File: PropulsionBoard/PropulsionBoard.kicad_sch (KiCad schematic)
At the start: 0 parts

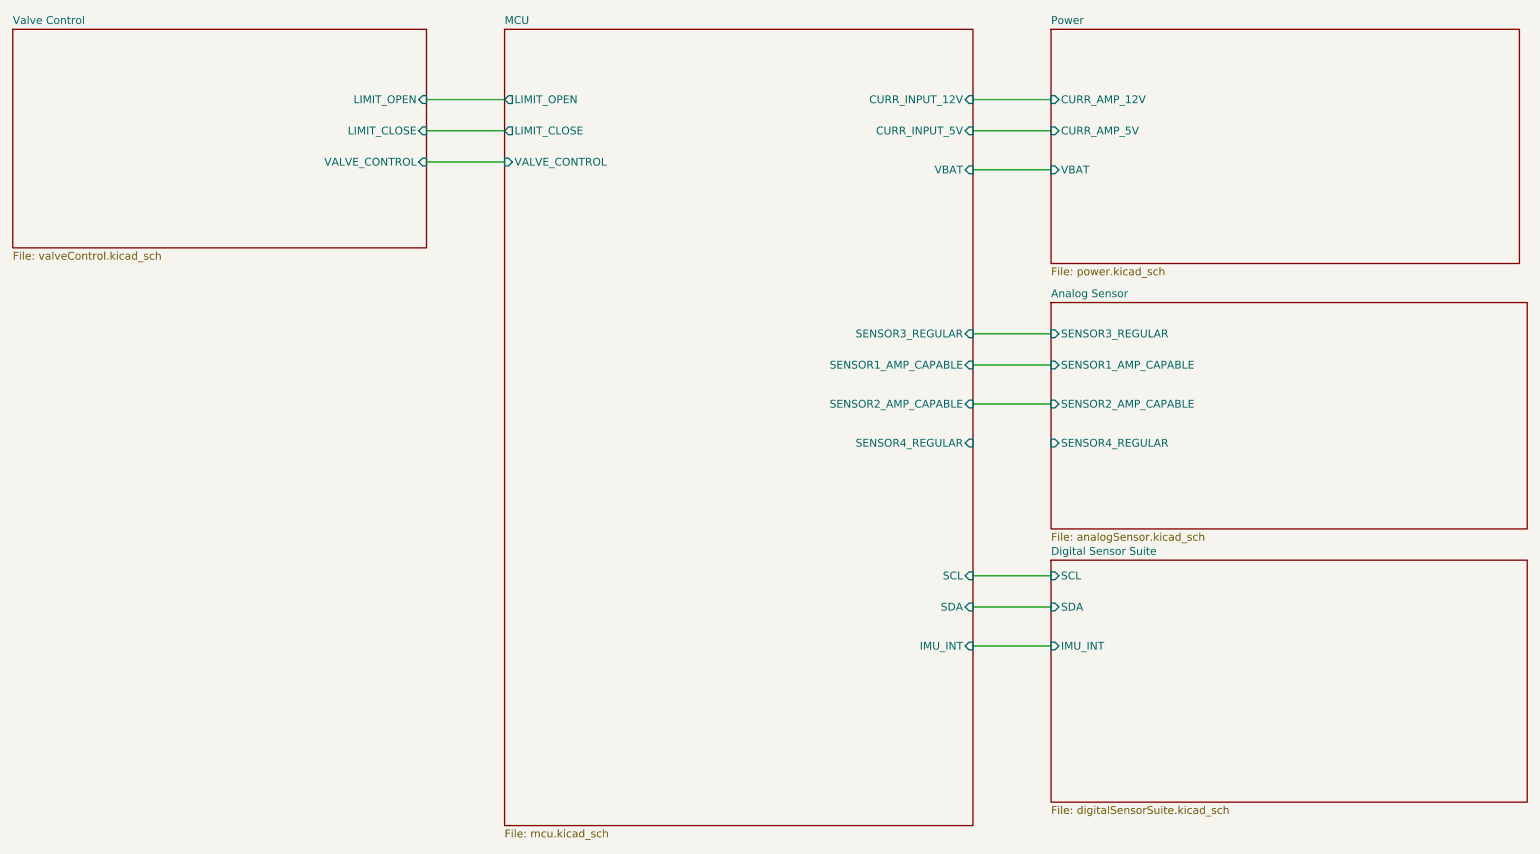
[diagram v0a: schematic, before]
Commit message: propulsion board address second review changes
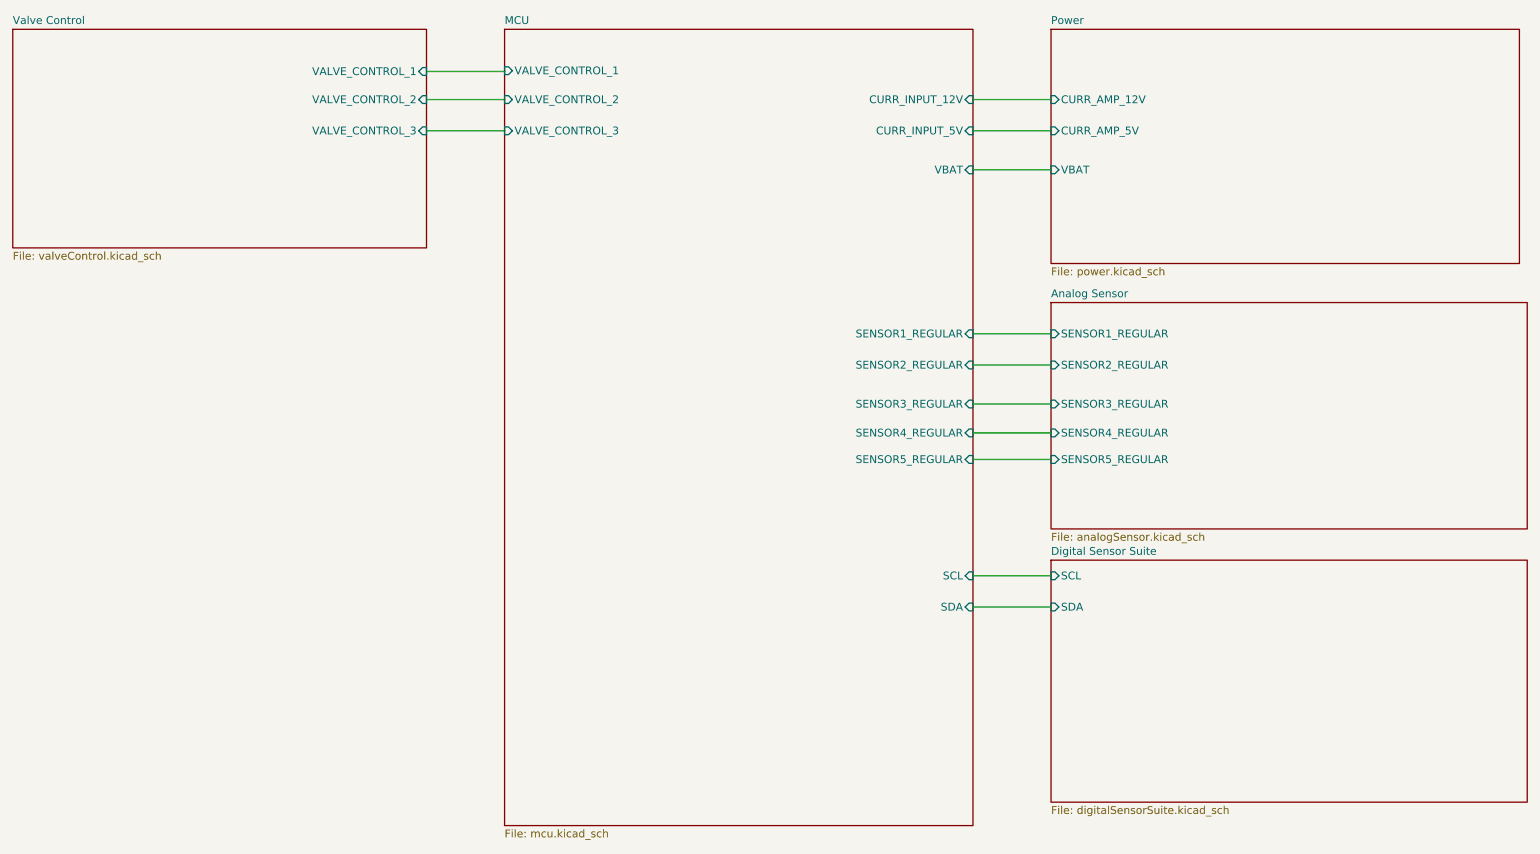
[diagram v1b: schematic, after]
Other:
- sheet Analog Sensor ports: added SENSOR1_REGULAR, SENSOR2_REGULAR, SENSOR5_REGULAR; removed SENSOR1_AMP_CAPABLE, SENSOR2_AMP_CAPABLE
- sheet Digital Sensor Suite ports: added none; removed IMU_INT
- sheet MCU ports: added SENSOR1_REGULAR, SENSOR2_REGULAR, SENSOR5_REGULAR, VALVE_CONTROL_1, VALVE_CONTROL_2, VALVE_CONTROL_3; removed IMU_INT, LIMIT_CLOSE, LIMIT_OPEN, SENSOR1_AMP_CAPABLE, SENSOR2_AMP_CAPABLE, VALVE_CONTROL
- sheet Valve Control ports: added VALVE_CONTROL_1, VALVE_CONTROL_2, VALVE_CONTROL_3; removed LIMIT_CLOSE, LIMIT_OPEN, VALVE_CONTROL
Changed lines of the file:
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@@
+    (stroke (width 0) (type default))
+  )
+  (wire (pts (xy 184.15 95.377) (xy 196.85 95.377))
+    (stroke (width 0) (type default))
+  )
+  (wire (pts (xy 184.15 91.059) (xy 196.85 91.059))
     (stroke (width 0) (type default))
   )
@@
   )
   (wire (pts (xy 184.15 36.83) (xy 196.85 36.83))
+    (stroke (width 0) (type default))
+  )
+  (wire (pts (xy 107.95 32.258) (xy 107.95 32.131))
     (stroke (width 0) (type default))
   )
@@
     (stroke (width 0) (type default))
   )
-  (wire (pts (xy 95.25 46.99) (xy 107.95 46.99))
-    (stroke (width 0) (type default))
-  )
-  (wire (pts (xy 184.15 125.73) (xy 196.85 125.73))
+  (wire (pts (xy 95.25 32.258) (xy 107.95 32.258))
     (stroke (width 0) (type default))
   )
@@
     (property "Sheetfile" "digitalSensorSuite.kicad_sch" (at 196.85 151.7146 0)
       (effects (font (size 1.27 1.27)) (justify left top))
-    )
-    (pin "IMU_INT" input (at 196.85 125.73 180)
-      (effects (font (size 1.27 1.27)) (justify left))
     )
     (pin "SDA" input (at 196.85 119.38 180)
@@
       (effects (font (size 1.27 1.27)) (justify left top))
     )
-    (pin "VALVE_CONTROL" input (at 95.25 46.99 0)
+    (pin "VALVE_CONTROL_3" input (at 95.25 41.91 0)
       (effects (font (size 1.27 1.27)) (justify right))
     )
-    (pin "LIMIT_OPEN" input (at 95.25 36.83 0)
+    (pin "VALVE_CONTROL_2" input (at 95.25 36.83 0)
       (effects (font (size 1.27 1.27)) (justify right))
     )
-    (pin "LIMIT_CLOSE" input (at 95.25 41.91 0)
+    (pin "VALVE_CONTROL_1" input (at 95.25 32.258 0)
       (effects (font (size 1.27 1.27)) (justify right))
     )
@@
       (effects (font (size 1.27 1.27)) hide)
     )
-    (pin "LIMIT_CLOSE" output (at 107.95 41.91 180)
-      (effects (font (size 1.27 1.27)) (justify left))
-    )
-    (pin "VALVE_CONTROL" input (at 107.95 46.99 180)
-      (effects (font (size 1.27 1.27)) (justify left))
-    )
-    (pin "SENSOR3_REGULAR" input (at 184.15 74.93 0)
+    (pin "SENSOR1_REGULAR" input (at 184.15 74.93 0)
       (effects (font (size 1.27 1.27)) (justify right))
     )
-    (pin "SENSOR1_AMP_CAPABLE" input (at 184.15 80.01 0)
+    (pin "SENSOR2_REGULAR" input (at 184.15 80.01 0)
       (effects (font (size 1.27 1.27)) (justify right))
     )
-    (pin "SENSOR2_AMP_CAPABLE" input (at 184.15 86.36 0)
+    (pin "SENSOR3_REGULAR" input (at 184.15 86.36 0)
       (effects (font (size 1.27 1.27)) (justify right))
     )
-    (pin "SENSOR4_REGULAR" input (at 184.15 92.71 0)
+    (pin "SENSOR4_REGULAR" input (at 184.15 91.059 0)
       (effects (font (size 1.27 1.27)) (justify right))
     )
@@
       (effects (font (size 1.27 1.27)) (justify right))
     )
-    (pin "IMU_INT" input (at 184.15 125.73 0)
+    (pin "VALVE_CONTROL_3" input (at 107.95 41.91 180)
+      (effects (font (size 1.27 1.27)) (justify left))
+    )
+    (pin "VALVE_CONTROL_2" input (at 107.95 36.83 180)
+      (effects (font (size 1.27 1.27)) (justify left))
+    )
+    (pin "VALVE_CONTROL_1" input (at 107.95 32.131 180)
+      (effects (font (size 1.27 1.27)) (justify left))
+    )
+    (pin "SENSOR5_REGULAR" input (at 184.15 95.377 0)
       (effects (font (size 1.27 1.27)) (justify right))
-    )
-    (pin "LIMIT_OPEN" output (at 107.95 36.83 180)
-      (effects (font (size 1.27 1.27)) (justify left))
     )
     (instances
@@
       (effects (font (size 1.27 1.27)) (justify left top))
     )
-    (pin "SENSOR1_AMP_CAPABLE" input (at 196.85 80.01 180)
+    (pin "SENSOR2_REGULAR" input (at 196.85 80.01 180)
       (effects (font (size 1.27 1.27)) (justify left))
     )
-    (pin "SENSOR3_REGULAR" input (at 196.85 74.93 180)
+    (pin "SENSOR1_REGULAR" input (at 196.85 74.93 180)
       (effects (font (size 1.27 1.27)) (justify left))
     )
-    (pin "SENSOR2_AMP_CAPABLE" input (at 196.85 86.36 180)
+    (pin "SENSOR3_REGULAR" input (at 196.85 86.36 180)
       (effects (font (size 1.27 1.27)) (justify left))
     )
-    (pin "SENSOR4_REGULAR" input (at 196.85 92.71 180)
+    (pin "SENSOR4_REGULAR" input (at 196.85 91.059 180)
       (effects (font (size 1.27 1.27)) (justify left))
     )
+    (pin "SENSOR5_REGULAR" input (at 196.85 95.377 180)
+      (effects (font (size 1.27 1.27)) (justify left))
+    )

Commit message: addressing latest comments
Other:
- sheet Analog Sensor ports: added SENSOR1, SENSOR2, SENSOR3, SENSOR4, SENSOR5, SENSOR6; removed SENSOR1_REGULAR, SENSOR2_REGULAR, SENSOR3_REGULAR, SENSOR4_REGULAR, SENSOR5_REGULAR
- sheet MCU ports: added SENSOR1, SENSOR2, SENSOR3, SENSOR4, SENSOR5, SENSOR6; removed SENSOR1_REGULAR, SENSOR2_REGULAR, SENSOR3_REGULAR, SENSOR4_REGULAR, SENSOR5_REGULAR
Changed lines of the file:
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@@
 (kicad_sch (version 20230121) (generator eeschema)
   (paper "A4")
-  (wire (pts (xy 184.15 80.01) (xy 196.85 80.01))
-    (stroke (width 0) (type default))
-  )
-  (wire (pts (xy 184.15 95.377) (xy 196.85 95.377))
-    (stroke (width 0) (type default))
-  )
-  (wire (pts (xy 184.15 91.059) (xy 196.85 91.059))
+  (wire (pts (xy 184.15 81.28) (xy 196.85 81.28))
+    (stroke (width 0) (type default))
+  )
+  (wire (pts (xy 184.15 91.44) (xy 196.85 91.44))
     (stroke (width 0) (type default))
   )
@@
     (stroke (width 0) (type default))
   )
-  (wire (pts (xy 184.15 74.93) (xy 196.85 74.93))
+  (wire (pts (xy 184.15 76.2) (xy 196.85 76.2))
     (stroke (width 0) (type default))
   )
@@
     (stroke (width 0) (type default))
   )
-  (wire (pts (xy 107.95 32.258) (xy 107.95 32.131))
-    (stroke (width 0) (type default))
-  )
   (wire (pts (xy 184.15 114.3) (xy 196.85 114.3))
     (stroke (width 0) (type default))
@@
     (stroke (width 0) (type default))
   )
+  (wire (pts (xy 184.15 101.6) (xy 196.85 101.6))
+    (stroke (width 0) (type default))
+  )
   (wire (pts (xy 184.15 48.26) (xy 196.85 48.26))
     (stroke (width 0) (type default))
   )
-  (wire (pts (xy 95.25 32.258) (xy 107.95 32.258))
+  (wire (pts (xy 95.25 31.75) (xy 107.95 31.75))
+    (stroke (width 0) (type default))
+  )
+  (wire (pts (xy 184.15 96.52) (xy 196.85 96.52))
     (stroke (width 0) (type default))
   )
@@
       (effects (font (size 1.27 1.27)) (justify right))
     )
-    (pin "VALVE_CONTROL_1" input (at 95.25 32.258 0)
+    (pin "VALVE_CONTROL_1" input (at 95.25 31.75 0)
       (effects (font (size 1.27 1.27)) (justify right))
     )
@@
       (effects (font (size 1.27 1.27)) hide)
     )
-    (pin "SENSOR1_REGULAR" input (at 184.15 74.93 0)
-      (effects (font (size 1.27 1.27)) (justify right))
-    )
-    (pin "SENSOR2_REGULAR" input (at 184.15 80.01 0)
-      (effects (font (size 1.27 1.27)) (justify right))
-    )
-    (pin "SENSOR3_REGULAR" input (at 184.15 86.36 0)
-      (effects (font (size 1.27 1.27)) (justify right))
-    )
-    (pin "SENSOR4_REGULAR" input (at 184.15 91.059 0)
+    (pin "SENSOR1" input (at 184.15 76.2 0)
+      (effects (font (size 1.27 1.27)) (justify right))
+    )
+    (pin "SENSOR2" input (at 184.15 81.28 0)
+      (effects (font (size 1.27 1.27)) (justify right))
+    )
+    (pin "SENSOR3" input (at 184.15 86.36 0)
+      (effects (font (size 1.27 1.27)) (justify right))
+    )
+    (pin "SENSOR4" input (at 184.15 91.44 0)
       (effects (font (size 1.27 1.27)) (justify right))
     )
@@
       (effects (font (size 1.27 1.27)) (justify left))
     )
-    (pin "VALVE_CONTROL_1" input (at 107.95 32.131 180)
-      (effects (font (size 1.27 1.27)) (justify left))
-    )
-    (pin "SENSOR5_REGULAR" input (at 184.15 95.377 0)
+    (pin "VALVE_CONTROL_1" input (at 107.95 31.75 180)
+      (effects (font (size 1.27 1.27)) (justify left))
+    )
+    (pin "SENSOR5" input (at 184.15 96.52 0)
+      (effects (font (size 1.27 1.27)) (justify right))
+    )
+    (pin "SENSOR6" input (at 184.15 101.6 0)
       (effects (font (size 1.27 1.27)) (justify right))
     )
@@
       (effects (font (size 1.27 1.27)) (justify left top))
     )
-    (pin "SENSOR2_REGULAR" input (at 196.85 80.01 180)
-      (effects (font (size 1.27 1.27)) (justify left))
-    )
-    (pin "SENSOR1_REGULAR" input (at 196.85 74.93 180)
-      (effects (font (size 1.27 1.27)) (justify left))
-    )
-    (pin "SENSOR3_REGULAR" input (at 196.85 86.36 180)
-      (effects (font (size 1.27 1.27)) (justify left))
-    )
-    (pin "SENSOR4_REGULAR" input (at 196.85 91.059 180)
-      (effects (font (size 1.27 1.27)) (justify left))
-    )
-    (pin "SENSOR5_REGULAR" input (at 196.85 95.377 180)
-      (effects (font (size 1.27 1.27)) (justify left))
-    )
+    (pin "SENSOR2" input (at 196.85 81.28 180)
+      (effects (font (size 1.27 1.27)) (justify left))
+    )
+    (pin "SENSOR1" input (at 196.85 76.2 180)
+      (effects (font (size 1.27 1.27)) (justify left))
+    )
+    (pin "SENSOR3" input (at 196.85 86.36 180)
+      (effects (font (size 1.27 1.27)) (justify left))
+    )
+    (pin "SENSOR4" input (at 196.85 91.44 180)
+      (effects (font (size 1.27 1.27)) (justify left))
+    )
+    (pin "SENSOR5" input (at 196.85 96.52 180)
+      (effects (font (size 1.27 1.27)) (justify left))
+    )
+    (pin "SENSOR6" input (at 196.85 101.6 180)
+      (effects (font (size 1.27 1.27)) (justify left))
+    )
